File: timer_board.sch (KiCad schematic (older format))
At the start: 1 part

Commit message: Put in more work on schematic
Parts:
- added C?: 1uF, ~, symbol C
- added CON?: AVR-ISP-6, AVR-ISP-6, symbol AVR-ISP-6
- added F?: FUSE, ~, symbol FUSE
- added P?: USBMICRO, symbol USBMICRO
- added R? (x4): 10k, ~, symbol R
- added R? (x2): 22, ~, symbol R
- added U?: DS3231N, symbol DS3231N
- added Y?: RESONATORSMD, ~, symbol RESONATORSMD
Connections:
- net labels added: +5V, GND, SCL, SDA, UVCC, reset
- wire segments 0 -> 59

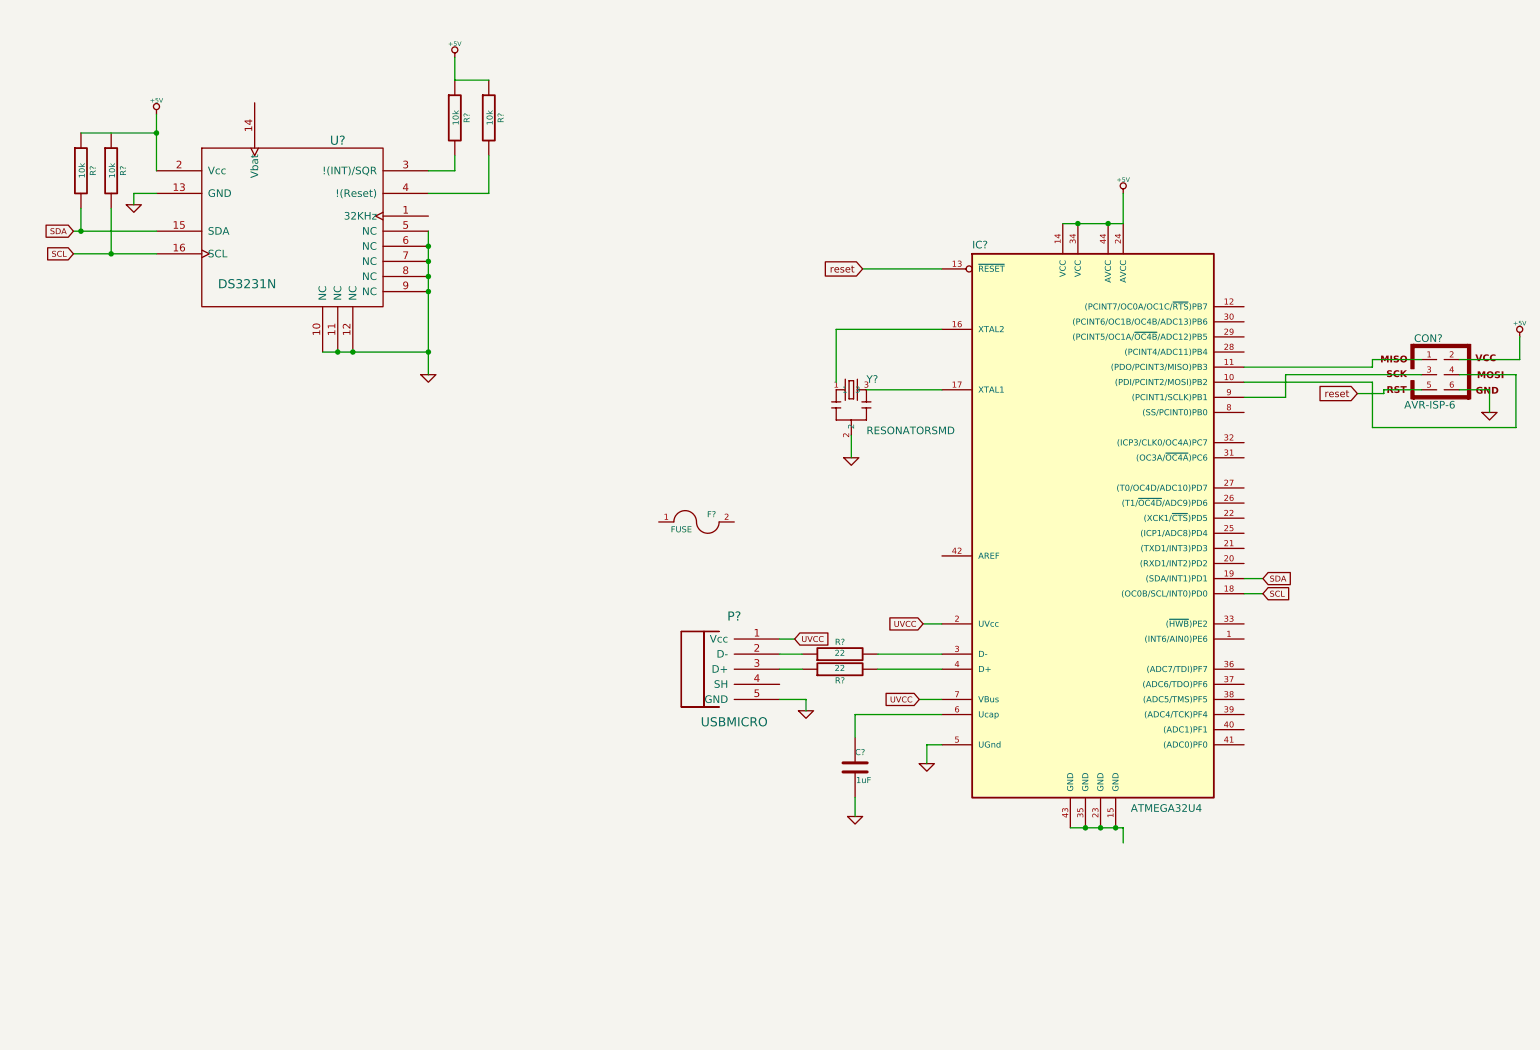
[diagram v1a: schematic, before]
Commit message: Added LCD and battery holder to schematic
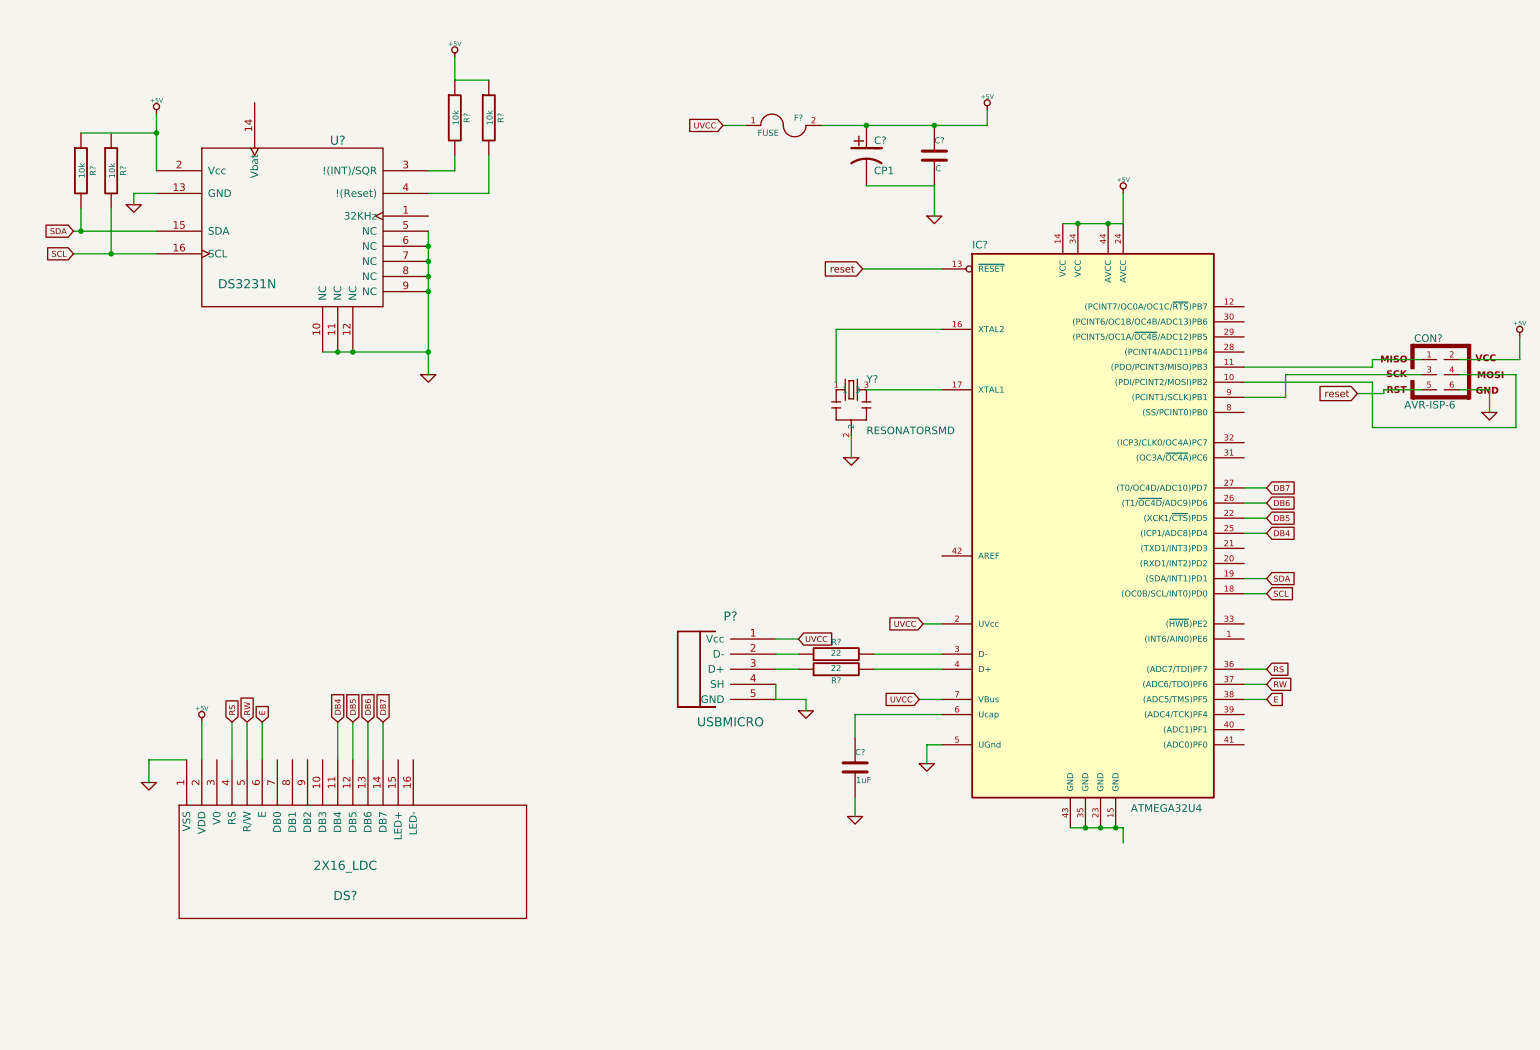
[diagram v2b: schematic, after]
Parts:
- added C?: CP1, ~, symbol CP1
- added C?: C, ~, symbol C
- added DS?: 2X16_LDC, symbol 2X16_LDC
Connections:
- net labels added: DB4, DB5, DB6, DB7, E, RS, RW
- wire segments 59 -> 82
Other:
- moved on the sheet: F?, P?, R?
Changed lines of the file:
@@
-EESchema Schematic File Version 2  date 6/22/2013 11:32:05 PM
+EESchema Schematic File Version 2  date 6/27/2013 10:45:44 PM
 LIBS:power
 LIBS:device
@@
 LIBS:custom_parts
 LIBS:Dispositivos_I2C
-LIBS:con-usb-3
 LIBS:timer_board-cache
 EELAYER 27 0
@@
 Sheet 1 1
 Title ""
-Date "23 jun 2013"
+Date "28 jun 2013"
 Rev ""
 Comp ""
@@
 Wire Wire Line
 	1350 1700 1500 1700
-Text GLabel 8825 4250 2    39   Input ~ 0
-SDA
-Text GLabel 8825 4350 2    39   Input ~ 0
-SCL
-Wire Wire Line
-	8825 4250 8700 4250
-Wire Wire Line
-	8700 4350 8825 4350
 Text GLabel 950  1950 0    39   Input ~ 0
 SDA
@@
 L USBMICRO P?
 U 1 1 51C68749
-P 5325 4800
-F 0 "P?" H 5325 5100 60  0000 C CNN
-F 1 "USBMICRO" H 5325 4400 60  0000 C CNN
-F 2 "" H 5175 4800 60  0000 C CNN
-F 3 "" H 5175 4800 60  0000 C CNN
-	1    5325 4800
+P 5300 4800
+F 0 "P?" H 5300 5100 60  0000 C CNN
+F 1 "USBMICRO" H 5300 4400 60  0000 C CNN
+F 2 "" H 5150 4800 60  0000 C CNN
+F 3 "" H 5150 4800 60  0000 C CNN
+	1    5300 4800
 	1    0    0    -1
 $EndComp
@@
 L R R?
 U 1 1 51C6875B
-P 6025 4750
-F 0 "R?" V 6105 4750 40  0000 C CNN
-F 1 "22" V 6032 4751 40  0000 C CNN
-F 2 "~" V 5955 4750 30  0000 C CNN
-F 3 "~" H 6025 4750 30  0000 C CNN
-	1    6025 4750
+P 6000 4750
+F 0 "R?" V 6080 4750 40  0000 C CNN
+F 1 "22" V 6007 4751 40  0000 C CNN
+F 2 "~" V 5930 4750 30  0000 C CNN
+F 3 "~" H 6000 4750 30  0000 C CNN
+	1    6000 4750
 	0    -1   -1   0
 $EndComp
@@
 L R R?
 U 1 1 51C68784
-P 6025 4850
-F 0 "R?" V 5950 4850 40  0000 C CNN
-F 1 "22" V 6032 4851 40  0000 C CNN
-F 2 "~" V 5955 4850 30  0000 C CNN
-F 3 "~" H 6025 4850 30  0000 C CNN
-	1    6025 4850
+P 6000 4850
+F 0 "R?" V 5925 4850 40  0000 C CNN
+F 1 "22" V 6007 4851 40  0000 C CNN
+F 2 "~" V 5930 4850 30  0000 C CNN
+F 3 "~" H 6000 4850 30  0000 C CNN
+	1    6000 4850
 	0    -1   -1   0
 $EndComp
-Wire Wire Line
-	5775 4750 5625 4750
-Wire Wire Line
-	5625 4850 5775 4850
-Wire Wire Line
-	6275 4750 6700 4750
-Wire Wire Line
-	6275 4850 6700 4850
 $Comp
 L FUSE F?
 U 1 1 51C688B3
-P 5075 3875
-F 0 "F?" H 5175 3925 40  0000 C CNN
-F 1 "FUSE" H 4975 3825 40  0000 C CNN
-F 2 "~" H 5075 3875 60  0000 C CNN
-F 3 "~" H 5075 3875 60  0000 C CNN
-	1    5075 3875
-	1    0    0    -1
-$EndComp
-Text GLabel 5725 4650 2    39   Input ~ 0
+P 5650 1250
+F 0 "F?" H 5750 1300 40  0000 C CNN
+F 1 "FUSE" H 5550 1200 40  0000 C CNN
+F 2 "~" H 5650 1250 60  0000 C CNN
+F 3 "~" H 5650 1250 60  0000 C CNN
+	1    5650 1250
+	1    0    0    -1
+$EndComp
+Text GLabel 5750 4650 2    39   Input ~ 0
 UVCC
-Wire Wire Line
-	5725 4650 5625 4650
 Text GLabel 6575 4550 0    39   Input ~ 0
 UVCC
@@
 $EndComp
 Wire Wire Line
-	5625 5050 5800 5050
-Wire Wire Line
 	5800 5050 5800 5125
 $Comp
@@
 Wire Wire Line
 	7900 1900 7900 1700
+Text GLabel 5250 1250 0    39   Input ~ 0
+UVCC
+Wire Wire Line
+	5400 1250 5250 1250
+$Comp
+L CP1 C?
+U 1 1 51CCFD2A
+P 6200 1450
+F 0 "C?" H 6250 1550 50  0000 L CNN
+F 1 "CP1" H 6250 1350 50  0000 L CNN
+F 2 "~" H 6200 1450 60  0000 C CNN
+F 3 "~" H 6200 1450 60  0000 C CNN
+	1    6200 1450
+	1    0    0    -1
+$EndComp
+$Comp
+L C C?
+U 1 1 51CCFD39
+P 6650 1450
+F 0 "C?" H 6650 1550 40  0000 L CNN
+F 1 "C" H 6656 1365 40  0000 L CNN
+F 2 "~" H 6688 1300 30  0000 C CNN
+F 3 "~" H 6650 1450 60  0000 C CNN
+	1    6650 1450
+	1    0    0    -1
+$EndComp
+Wire Wire Line
+	5900 1250 7000 1250
+Connection ~ 6200 1250
+Wire Wire Line
+	6650 1650 6200 1650
+$Comp
+L GND #PWR?
+U 1 1 51CCFE2D
+P 6650 1850
+F 0 "#PWR?" H 6650 1850 30  0001 C CNN
+F 1 "GND" H 6650 1780 30  0001 C CNN
+F 2 "" H 6650 1850 60  0000 C CNN
+F 3 "" H 6650 1850 60  0000 C CNN
+	1    6650 1850
+	1    0    0    -1
+$EndComp
+Wire Wire Line
+	6650 1650 6650 1850
+$Comp
+L +5V #PWR?
+U 1 1 51CCFE82
+P 7000 1150
+F 0 "#PWR?" H 7000 1240 20  0001 C CNN
+F 1 "+5V" H 7000 1240 30  0000 C CNN
+F 2 "" H 7000 1150 60  0000 C CNN
+F 3 "" H 7000 1150 60  0000 C CNN
+	1    7000 1150
+	1    0    0    -1
+$EndComp
+Wire Wire Line
+	7000 1250 7000 1150
+Connection ~ 6650 1250
+Wire Wire Line
+	5750 4650 5600 4650
+Wire Wire Line
+	5750 4750 5600 4750
+Wire Wire Line
+	5750 4850 5600 4850
+Wire Wire Line
+	5600 4950 5600 5050
+Wire Wire Line
+	5600 5050 5800 5050
+Wire Wire Line
+	6700 4750 6250 4750
+Wire Wire Line
+	6700 4850 6250 4850
+$Comp
+L 2X16_LDC DS?
+U 1 1 51CD1203
+P 2750 6000
+F 0 "DS?" H 2750 5650 60  0000 C CNN
+F 1 "2X16_LDC" H 2750 5850 60  0000 C CNN
+F 2 "" H 2750 6000 60  0000 C CNN
+F 3 "" H 2750 6000 60  0000 C CNN
+	1    2750 6000
+	1    0    0    -1
+$EndComp
+$Comp
+L +5V #PWR?
+U 1 1 51CD1210
+P 1800 5200
+F 0 "#PWR?" H 1800 5290 20  0001 C CNN
+F 1 "+5V" H 1800 5290 30  0000 C CNN
+F 2 "" H 1800 5200 60  0000 C CNN
+F 3 "" H 1800 5200 60  0000 C CNN
+	1    1800 5200
+	1    0    0    -1
+$EndComp
+Wire Wire Line
+	1800 5200 1800 5450
+$Comp
+L GND #PWR?
+U 1 1 51CD126A
+P 1450 5600
+F 0 "#PWR?" H 1450 5600 30  0001 C CNN
+F 1 "GND" H 1450 5530 30  0001 C CNN
+F 2 "" H 1450 5600 60  0000 C CNN
+F 3 "" H 1450 5600 60  0000 C CNN
+	1    1450 5600
+	1    0    0    -1
+$EndComp
+Wire Wire Line
+	1700 5450 1450 5450
+Wire Wire Line
+	1450 5450 1450 5600
+Text GLabel 2700 5200 1    39   Input ~ 0
+DB4
+Text GLabel 2800 5200 1    39   Input ~ 0
+DB5
+Text GLabel 2900 5200 1    39   Input ~ 0
+DB6
+Text GLabel 3000 5200 1    39   Input ~ 0
+DB7
+Wire Wire Line
+	2700 5200 2700 5450
+Wire Wire Line
+	2800 5200 2800 5450
+Wire Wire Line
+	2900 5200 2900 5450
+Wire Wire Line
+	3000 5200 3000 5450
+Text GLabel 8850 3950 2    39   Input ~ 0
+DB4
+Wire Wire Line
+	8850 3950 8700 3950
+Text GLabel 8850 4250 2    39   Input ~ 0
+SDA
+Text GLabel 8850 4350 2    39   Input ~ 0
+SCL
+Wire Wire Line
+	8850 4250 8700 4250
+Wire Wire Line
+	8700 4350 8850 4350
+Text GLabel 8850 3850 2    39   Input ~ 0
+DB5
+Text GLabel 8850 3750 2    39   Input ~ 0
+DB6
+Text GLabel 8850 3650 2    39   Input ~ 0
+DB7
+Wire Wire Line
+	8850 3850 8700 3850
+Wire Wire Line
+	8700 3750 8850 3750
+Wire Wire Line
+	8700 3650 8850 3650
+Text GLabel 2100 5200 1    39   Input ~ 0
+RW
+Text GLabel 2200 5200 1    39   Input ~ 0
+E
+Text GLabel 2000 5200 1    39   Input ~ 0
+RS
+Wire Wire Line
+	2000 5200 2000 5450
+Wire Wire Line
+	2100 5200 2100 5450
+Wire Wire Line
+	2200 5200 2200 5450
+Text GLabel 8850 4850 2    39   Input ~ 0
+RS
+Text GLabel 8850 4950 2    39   Input ~ 0
+RW
+Text GLabel 8850 5050 2    39   Input ~ 0
+E
+Wire Wire Line
+	8850 4850 8700 4850
+Wire Wire Line
+	8700 4950 8850 4950
+Wire Wire Line
+	8700 5050 8850 5050
 $EndSCHEMATC

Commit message: forgot to save
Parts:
- added BT?: BATTERY, ~, symbol BATTERY
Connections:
- net GND: now also BT?.2 (-)
- net at U?.14 (Vbat): now also BT?.1 (+)
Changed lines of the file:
@@
-EESchema Schematic File Version 2  date 6/27/2013 10:45:44 PM
+EESchema Schematic File Version 2  date 6/27/2013 10:57:25 PM
 LIBS:power
 LIBS:device
@@
 Wire Wire Line
 	8700 5050 8850 5050
+$Comp
+L BATTERY BT?
+U 1 1 51CD1CCB
+P 2450 750
+F 0 "BT?" H 2450 950 50  0000 C CNN
+F 1 "BATTERY" H 2450 560 50  0000 C CNN
+F 2 "~" H 2450 750 60  0000 C CNN
+F 3 "~" H 2450 750 60  0000 C CNN
+	1    2450 750
+	1    0    0    -1
+$EndComp
+Wire Wire Line
+	2150 750  2150 1100
+$Comp
+L GND #PWR?
+U 1 1 51CD1D3C
+P 2850 850
+F 0 "#PWR?" H 2850 850 30  0001 C CNN
+F 1 "GND" H 2850 780 30  0001 C CNN
+F 2 "" H 2850 850 60  0000 C CNN
+F 3 "" H 2850 850 60  0000 C CNN
+	1    2850 850
+	1    0    0    -1
+$EndComp
+Wire Wire Line
+	2750 750  2850 750
+Wire Wire Line
+	2850 750  2850 850
 $EndSCHEMATC
